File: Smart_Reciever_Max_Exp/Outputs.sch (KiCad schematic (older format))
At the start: 8 parts, among them J2 Expansion Header, J4 EXT2, U5 74LS125, U6 74LS125, U7 74LS125

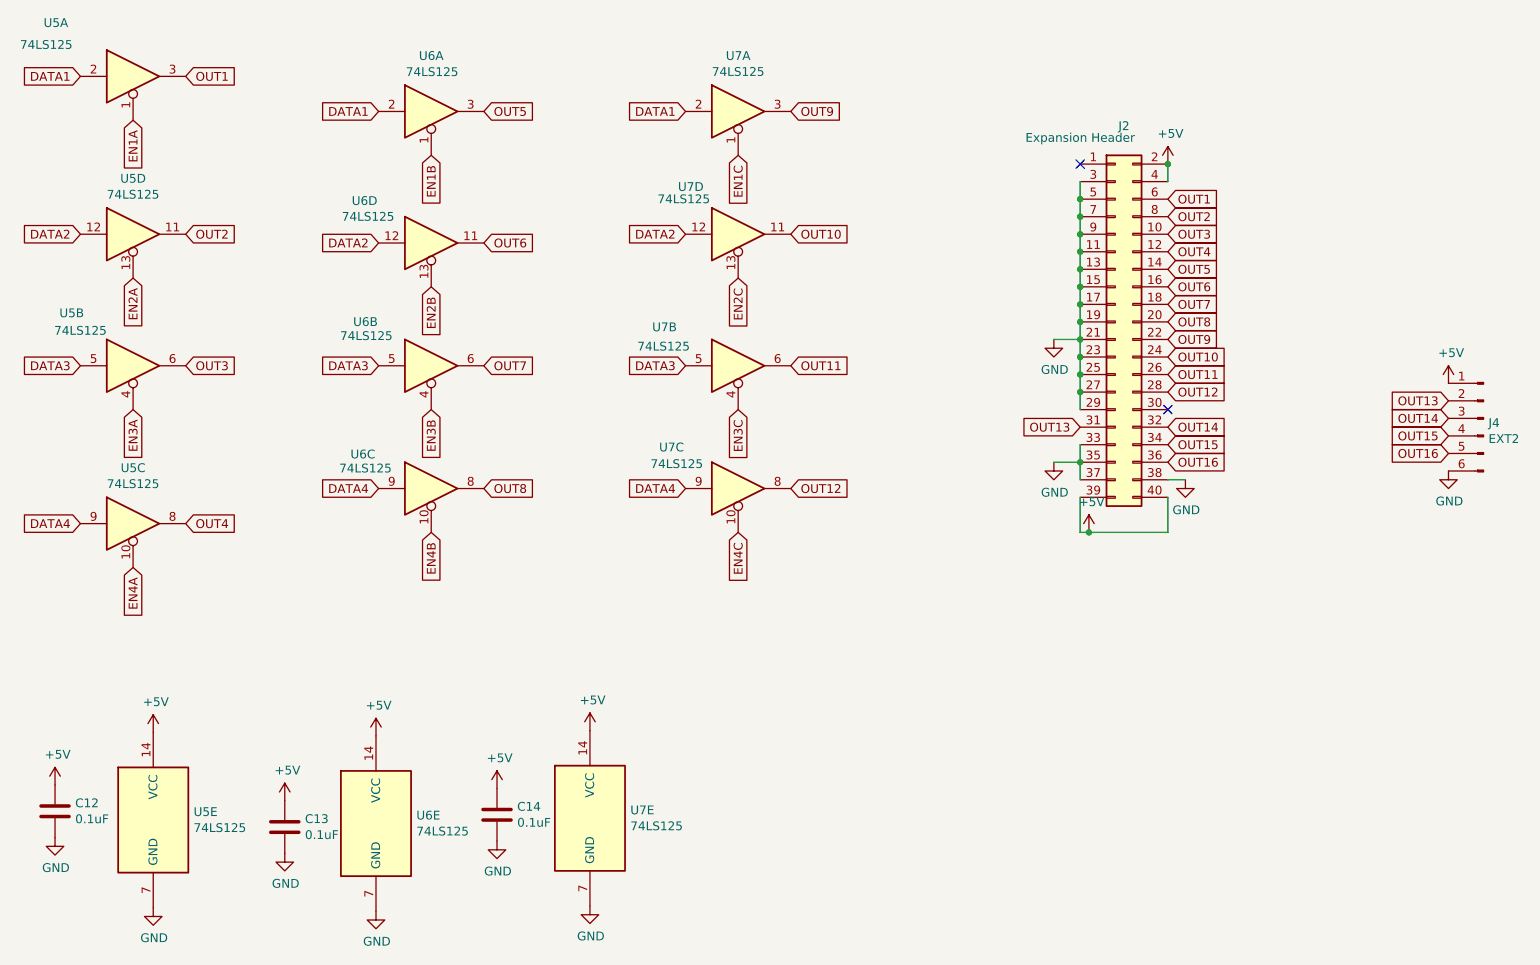
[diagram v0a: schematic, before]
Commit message: renumber components
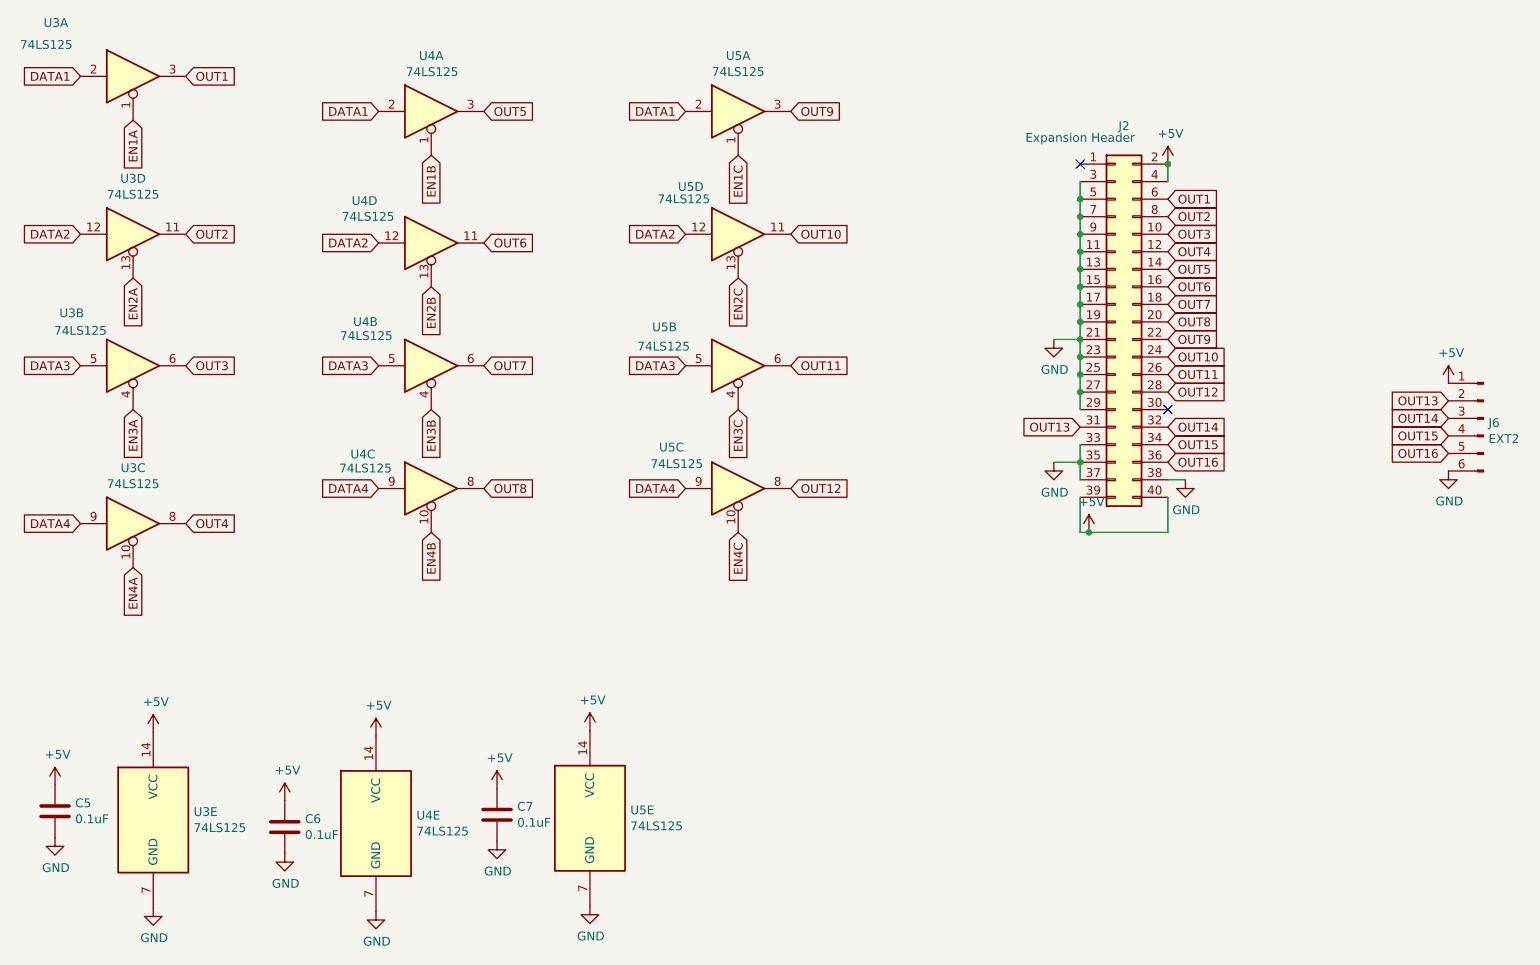
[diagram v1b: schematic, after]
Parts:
- renumbered C12 to C5, C13 to C6, J4 to J6, U5 to U3, U6 to U4, U7 to U5
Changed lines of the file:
@@
 $EndDescr
 $Comp
-L 74xx:74LS125 U5
+L 74xx:74LS125 U3
 U 1 1 5FF31072
 P 2450 2000
-F 0 "U5" H 2010 2305 50  0000 C CNN
+F 0 "U3" H 2010 2305 50  0000 C CNN
 F 1 "74LS125" H 1955 2180 50  0000 C CNN
 F 2 "Package_DIP:DIP-14_W7.62mm_LongPads" H 2450 2000 50  0001 C CNN
@@
 $EndComp
 $Comp
-L 74xx:74LS125 U5
+L 74xx:74LS125 U3
 U 3 1 5FF33181
 P 2450 4550
-F 0 "U5" H 2450 4867 50  0000 C CNN
+F 0 "U3" H 2450 4867 50  0000 C CNN
 F 1 "74LS125" H 2450 4776 50  0000 C CNN
 F 2 "Package_DIP:DIP-14_W7.62mm_LongPads" H 2450 4550 50  0001 C CNN
@@
 $EndComp
 $Comp
-L 74xx:74LS125 U5
+L 74xx:74LS125 U3
 U 4 1 5FF33C96
 P 2450 2900
-F 0 "U5" H 2450 3217 50  0000 C CNN
+F 0 "U3" H 2450 3217 50  0000 C CNN
 F 1 "74LS125" H 2450 3126 50  0000 C CNN
 F 2 "Package_DIP:DIP-14_W7.62mm_LongPads" H 2450 2900 50  0001 C CNN
@@
 $EndComp
 $Comp
-L 74xx:74LS125 U6
+L 74xx:74LS125 U4
 U 5 1 5FF350CB
 P 3835 6260
-F 0 "U6" H 4065 6306 50  0000 L CNN
+F 0 "U4" H 4065 6306 50  0000 L CNN
 F 1 "74LS125" H 4065 6215 50  0000 L CNN
 F 2 "Package_DIP:DIP-14_W7.62mm_LongPads" H 3835 6260 50  0001 C CNN
@@
 AR Path="/5D4CFBF5" Ref="C?"  Part="1"
 AR Path="/5D469293/5D4CFBF5" Ref="C3"  Part="1"
-AR Path="/5FF30D74/5D4CFBF5" Ref="C14"  Part="1"
-F 0 "C14" H 4640 6256 50  0000 L CNN
+AR Path="/5FF30D74/5D4CFBF5" Ref="C7"  Part="1"
+F 0 "C7" H 4640 6256 50  0000 L CNN
 F 1 "0.1uF" H 4640 6165 50  0000 L CNN
 F 2 "Capacitor_THT:C_Rect_L7.0mm_W2.0mm_P5.00mm" H 4563 6060 50  0001 C CNN
@@
 $EndComp
 $Comp
-L 74xx:74LS125 U6
+L 74xx:74LS125 U4
 U 1 1 5FFD2711
 P 4150 2200
-F 0 "U6" H 4150 2517 50  0000 C CNN
+F 0 "U4" H 4150 2517 50  0000 C CNN
 F 1 "74LS125" H 4155 2425 50  0000 C CNN
 F 2 "Package_DIP:DIP-14_W7.62mm_LongPads" H 4150 2200 50  0001 C CNN
@@
 $EndComp
 $Comp
-L 74xx:74LS125 U6
+L 74xx:74LS125 U4
 U 2 1 5FFD2717
 P 4150 3650
-F 0 "U6" H 3775 3900 50  0000 C CNN
+F 0 "U4" H 3775 3900 50  0000 C CNN
 F 1 "74LS125" H 3780 3820 50  0000 C CNN
 F 2 "Package_DIP:DIP-14_W7.62mm_LongPads" H 4150 3650 50  0001 C CNN
@@
 $EndComp
 $Comp
-L 74xx:74LS125 U6
+L 74xx:74LS125 U4
 U 3 1 5FFD271D
 P 4150 4350
-F 0 "U6" H 3760 4545 50  0000 C CNN
+F 0 "U4" H 3760 4545 50  0000 C CNN
 F 1 "74LS125" H 3775 4465 50  0000 C CNN
 F 2 "Package_DIP:DIP-14_W7.62mm_LongPads" H 4150 4350 50  0001 C CNN
@@
 $EndComp
 $Comp
-L 74xx:74LS125 U6
+L 74xx:74LS125 U4
 U 4 1 5FFD2723
 P 4150 2950
-F 0 "U6" H 3770 3190 50  0000 C CNN
+F 0 "U4" H 3770 3190 50  0000 C CNN
 F 1 "74LS125" H 3790 3100 50  0000 C CNN
 F 2 "Package_DIP:DIP-14_W7.62mm_LongPads" H 4150 2950 50  0001 C CNN
@@
 $EndComp
 $Comp
-L 74xx:74LS125 U7
+L 74xx:74LS125 U5
 U 5 1 5FFD2729
 P 5055 6230
-F 0 "U7" H 5285 6276 50  0000 L CNN
+F 0 "U5" H 5285 6276 50  0000 L CNN
 F 1 "74LS125" H 5285 6185 50  0000 L CNN
 F 2 "Package_DIP:DIP-14_W7.62mm_LongPads" H 5055 6230 50  0001 C CNN
@@
 $EndComp
 $Comp
-L 74xx:74LS125 U7
+L 74xx:74LS125 U5
 U 1 1 5FFD8497
 P 5900 2200
-F 0 "U7" H 5900 2517 50  0000 C CNN
+F 0 "U5" H 5900 2517 50  0000 C CNN
 F 1 "74LS125" H 5900 2426 50  0000 C CNN
 F 2 "Package_DIP:DIP-14_W7.62mm_LongPads" H 5900 2200 50  0001 C CNN
@@
 $EndComp
 $Comp
-L 74xx:74LS125 U7
+L 74xx:74LS125 U5
 U 2 1 5FFD849D
 P 5900 3650
-F 0 "U7" H 5480 3870 50  0000 C CNN
+F 0 "U5" H 5480 3870 50  0000 C CNN
 F 1 "74LS125" H 5475 3760 50  0000 C CNN
 F 2 "Package_DIP:DIP-14_W7.62mm_LongPads" H 5900 3650 50  0001 C CNN
@@
 $EndComp
 $Comp
-L 74xx:74LS125 U7
+L 74xx:74LS125 U5
 U 3 1 5FFD84A3
 P 5900 4350
-F 0 "U7" H 5520 4585 50  0000 C CNN
+F 0 "U5" H 5520 4585 50  0000 C CNN
 F 1 "74LS125" H 5550 4490 50  0000 C CNN
 F 2 "Package_DIP:DIP-14_W7.62mm_LongPads" H 5900 4350 50  0001 C CNN
@@
 $EndComp
 $Comp
-L 74xx:74LS125 U7
+L 74xx:74LS125 U5
 U 4 1 5FFD84A9
 P 5900 2900
-F 0 "U7" H 5630 3170 50  0000 C CNN
+F 0 "U5" H 5630 3170 50  0000 C CNN
 F 1 "74LS125" H 5590 3100 50  0000 C CNN
 F 2 "Package_DIP:DIP-14_W7.62mm_LongPads" H 5900 2900 50  0001 C CNN
@@
 AR Path="/6006A2A1" Ref="C?"  Part="1"
 AR Path="/5D469293/6006A2A1" Ref="C?"  Part="1"
-AR Path="/5FF30D74/6006A2A1" Ref="C12"  Part="1"
-F 0 "C12" H 2120 6236 50  0000 L CNN
+AR Path="/5FF30D74/6006A2A1" Ref="C5"  Part="1"
+F 0 "C5" H 2120 6236 50  0000 L CNN
 F 1 "0.1uF" H 2120 6145 50  0000 L CNN
 F 2 "Capacitor_THT:C_Rect_L7.0mm_W2.0mm_P5.00mm" H 2043 6040 50  0001 C CNN
@@
 AR Path="/6006B239" Ref="C?"  Part="1"
 AR Path="/5D469293/6006B239" Ref="C?"  Part="1"
-AR Path="/5FF30D74/6006B239" Ref="C13"  Part="1"
-F 0 "C13" H 3430 6326 50  0000 L CNN
+AR Path="/5FF30D74/6006B239" Ref="C6"  Part="1"
+F 0 "C6" H 3430 6326 50  0000 L CNN
 F 1 "0.1uF" H 3430 6235 50  0000 L CNN
 F 2 "Capacitor_THT:C_Rect_L7.0mm_W2.0mm_P5.00mm" H 3353 6130 50  0001 C CNN
@@
 $EndComp
 $Comp
-L 74xx:74LS125 U5
+L 74xx:74LS125 U3
 U 5 1 5FFD84AF
 P 2565 6240
-F 0 "U5" H 2795 6286 50  0000 L CNN
+F 0 "U3" H 2795 6286 50  0000 L CNN
 F 1 "74LS125" H 2795 6195 50  0000 L CNN
 F 2 "Package_DIP:DIP-14_W7.62mm_LongPads" H 2565 6240 50  0001 C CNN
@@
 OUT12
 $Comp
-L 74xx:74LS125 U5
+L 74xx:74LS125 U3
 U 2 1 5FF3245C
 P 2450 3650
-F 0 "U5" H 2100 3950 50  0000 C CNN
+F 0 "U3" H 2100 3950 50  0000 C CNN
 F 1 "74LS125" H 2150 3850 50  0000 C CNN
 F 2 "Package_DIP:DIP-14_W7.62mm_LongPads" H 2450 3650 50  0001 C CNN
@@
 $EndComp
 $Comp
-L Connector:Conn_01x06_Male J4
+L Connector:Conn_01x06_Male J6
 U 1 1 60230DA3
 P 10150 3950
-F 0 "J4" H 10122 3924 50  0000 R CNN
+F 0 "J6" H 10122 3924 50  0000 R CNN
 F 1 "EXT2" H 10122 3833 50  0000 R CNN
 F 2 "Connector_PinHeader_2.54mm:PinHeader_1x06_P2.54mm_Vertical" H 10150 3950 50  0001 C CNN
